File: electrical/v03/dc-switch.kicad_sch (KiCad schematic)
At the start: 26 parts, among them J201 48V DC INPUT, U306 TPS3808G01DBVR, U307 SN74LVC1G17DBVR, U401 TPS26631PWPR

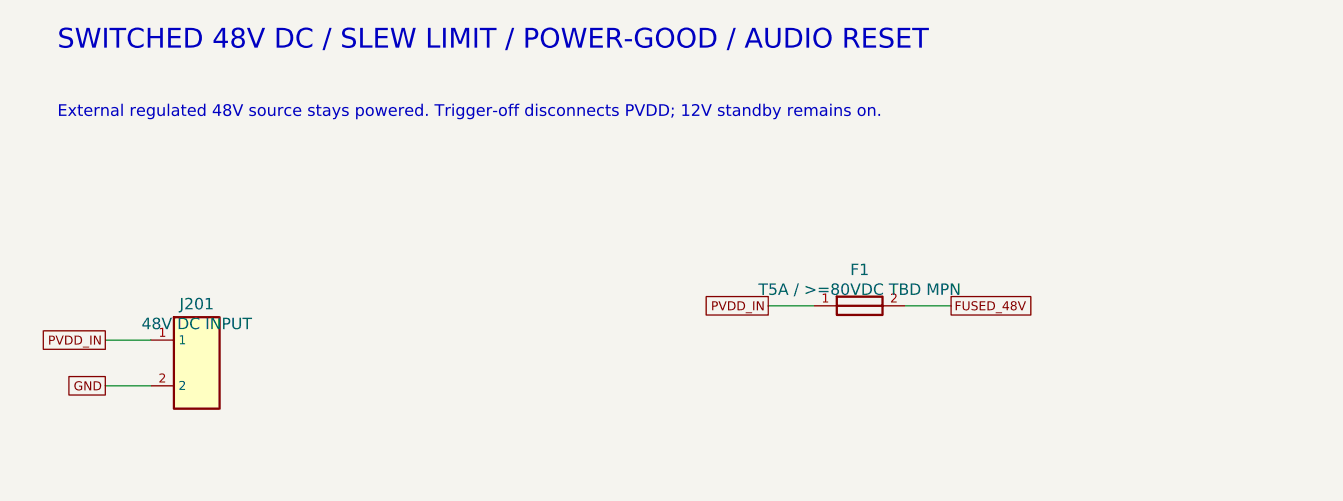
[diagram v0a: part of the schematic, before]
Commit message: Plan internal dual supplies with a single mains inlet
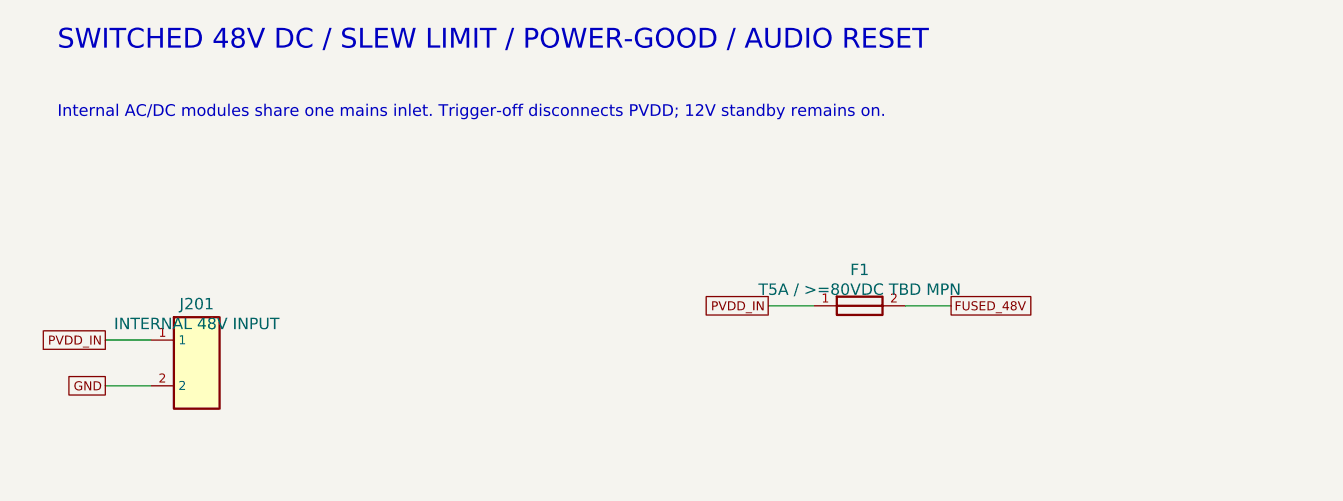
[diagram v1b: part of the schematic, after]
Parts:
- J201: value 48V DC INPUT -> INTERNAL 48V INPUT
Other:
- note added: "Internal AC/DC modules share one mains inlet. Trigger-off disconnects PVDD; 12V standby remains on."
- note removed: "External regulated 48V source stays powered. Trigger-off disconnects PVDD; 12V standby remains on."

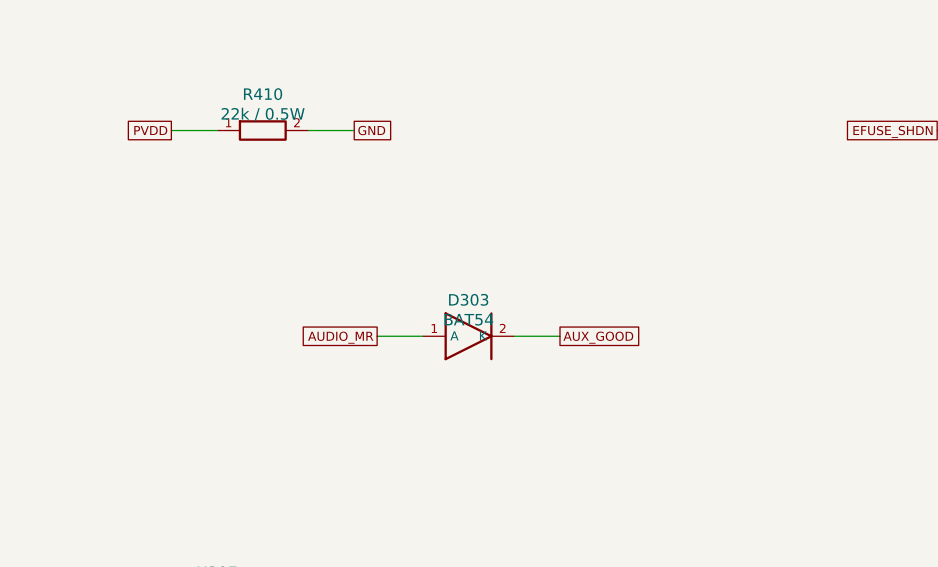
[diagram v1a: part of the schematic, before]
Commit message: Start unrouted PCB placement and correct BAT54 package pin mapping
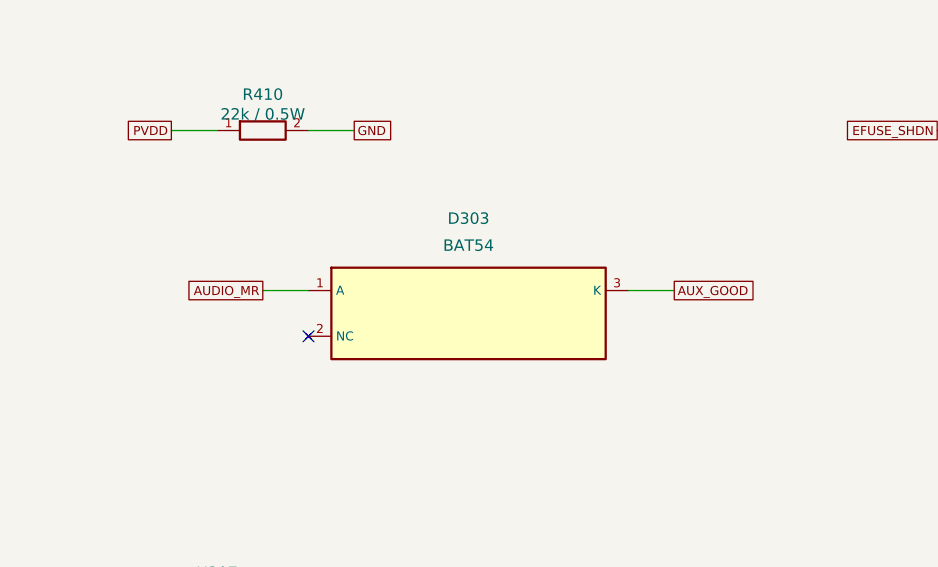
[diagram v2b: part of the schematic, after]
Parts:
- D303: symbol Project:Diode -> Project:BAT54
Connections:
- net AUX_GOOD: now also D303.3 (K); no longer D303.2 (K)
- no-connect marks 6 -> 7
